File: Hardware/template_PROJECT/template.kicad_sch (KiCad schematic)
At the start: 7 parts

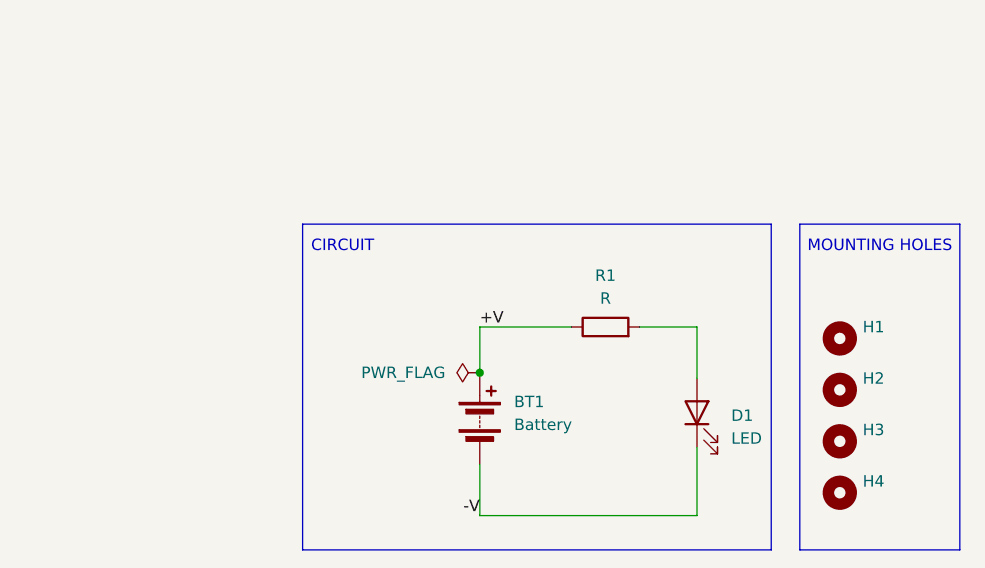
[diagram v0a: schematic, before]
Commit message: excluded mounting holes from bom and has an erc error i want to see what happens
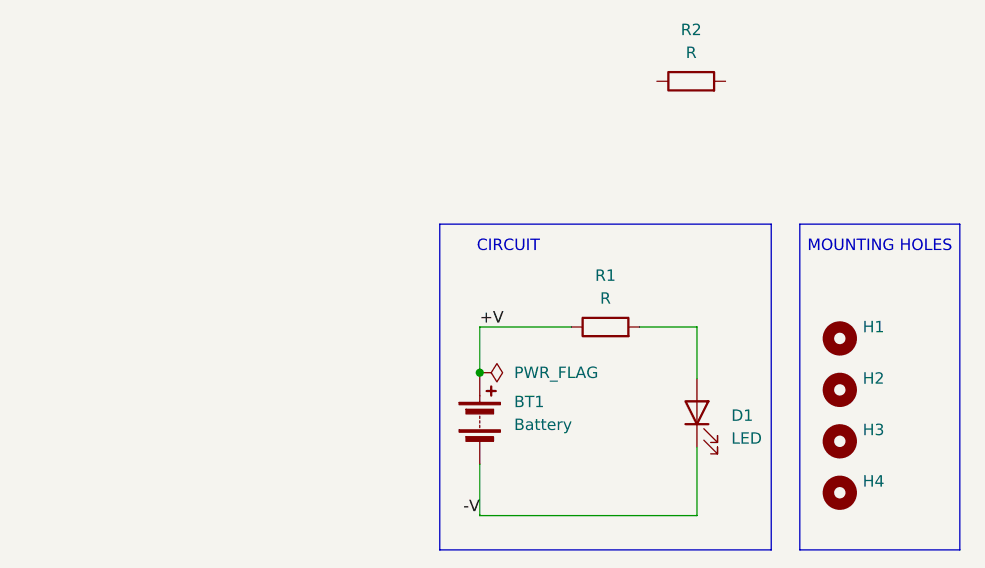
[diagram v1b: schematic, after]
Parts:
- added R2: R, Resistor_SMD:R_0805_2012Metric, symbol Device:R
- H1, H2, H3, H4: now left out of the parts list
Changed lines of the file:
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@@
 	)
 	(rectangle
-		(start 112.395 80.645)
+		(start 127.635 80.645)
 		(end 164.465 116.84)
 		(stroke
@@
 	(text "CIRCUIT"
 		(exclude_from_sim no)
-		(at 116.84 83.185 0)
+		(at 135.255 83.185 0)
 		(effects
 			(font
@@
 		(unit 1)
 		(exclude_from_sim no)
-		(in_bom yes)
+		(in_bom no)
 		(on_board yes)
 		(dnp no)
@@
 		(unit 1)
 		(exclude_from_sim no)
-		(in_bom yes)
+		(in_bom no)
 		(on_board yes)
 		(dnp no)
@@
 	(symbol
 		(lib_id "power:PWR_FLAG")
-		(at 132.08 97.155 90)
+		(at 132.08 97.155 270)
 		(unit 1)
 		(exclude_from_sim no)
@@
 		(fields_autoplaced yes)
 		(property "Reference" "#FLG01"
-			(at 130.175 97.155 0)
+			(at 133.985 97.155 0)
 			(effects
 				(font
@@
 		)
 		(property "Value" "PWR_FLAG"
-			(at 128.27 97.1549 90)
+			(at 135.89 97.1549 90)
 			(effects
 				(font
@@
 		(unit 1)
 		(exclude_from_sim no)
-		(in_bom yes)
+		(in_bom no)
 		(on_board yes)
 		(dnp no)
@@
 	)
 	(symbol
+		(lib_id "Device:R")
+		(at 155.575 64.77 90)
+		(unit 1)
+		(exclude_from_sim no)
+		(in_bom yes)
+		(on_board yes)
+		(dnp no)
+		(fields_autoplaced yes)
+		(property "Reference" "R2"
+			(at 155.575 59.055 90)
+			(effects
+				(font
+					(size 1.27 1.27)
+				)
+			)
+		)
+		(property "Value" "R"
+			(at 155.575 61.595 90)
+			(effects
+				(font
+					(size 1.27 1.27)
+				)
+			)
+		)
+		(property "Footprint" "Resistor_SMD:R_0805_2012Metric"
+			(at 155.575 66.548 90)
+			(effects
+				(font
+					(size 1.27 1.27)
+				)
+				(hide yes)
+			)
+		)
+		(property "Datasheet" "~"
+			(at 155.575 64.77 0)
+			(effects
+				(font
+					(size 1.27 1.27)
+				)
+				(hide yes)
+			)
+		)
+		(property "Description" "Resistor"
+			(at 155.575 64.77 0)
+			(effects
+				(font
+					(size 1.27 1.27)
+				)
+				(hide yes)
+			)
+		)
+		(pin "1"
+		)
+		(pin "2"
+		)
+		(instances
+			(project "template"
+				(path "/92a86815-0425-4ac3-80bb-037195814139"
+					(reference "R2")
+					(unit 1)
+				)
+			)
+		)
+	)
+	(symbol
 		(lib_id "Mechanical:MountingHole")
 		(at 172.085 99.06 0)
 		(unit 1)
 		(exclude_from_sim no)
-		(in_bom yes)
-		(on_board yes)
-		(dnp no)
+		(in_bom no)
+		(on_board yes)
+		(dnp no)

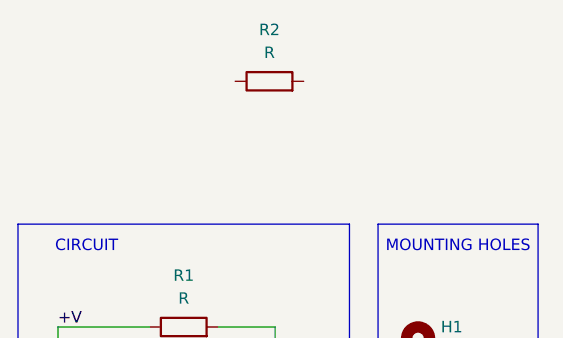
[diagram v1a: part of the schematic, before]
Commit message: should not longer error
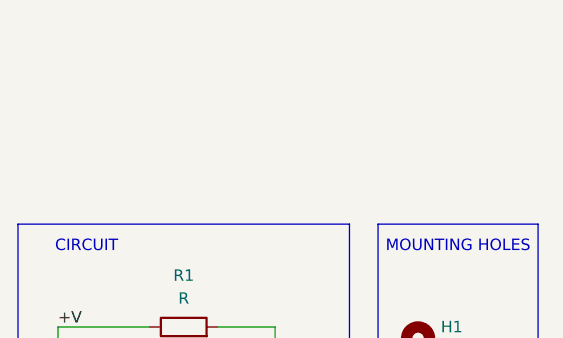
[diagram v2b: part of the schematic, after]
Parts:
- removed R2: R, Resistor_SMD:R_0805_2012Metric, symbol Device:R
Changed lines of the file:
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@@
-	)
-	(symbol
-		(lib_id "Device:R")
-		(at 155.575 64.77 90)
-		(unit 1)
-		(exclude_from_sim no)
-		(in_bom yes)
-		(on_board yes)
-		(dnp no)
-		(fields_autoplaced yes)
-		(property "Reference" "R2"
-			(at 155.575 59.055 90)
-			(effects
-				(font
-					(size 1.27 1.27)
-				)
-			)
-		)
-		(property "Value" "R"
-			(at 155.575 61.595 90)
-			(effects
-				(font
-					(size 1.27 1.27)
-				)
-			)
-		)
-		(property "Footprint" "Resistor_SMD:R_0805_2012Metric"
-			(at 155.575 66.548 90)
-			(effects
-				(font
-					(size 1.27 1.27)
-				)
-				(hide yes)
-			)
-		)
-		(property "Datasheet" "~"
-			(at 155.575 64.77 0)
-			(effects
-				(font
-					(size 1.27 1.27)
-				)
-				(hide yes)
-			)
-		)
-		(property "Description" "Resistor"
-			(at 155.575 64.77 0)
-			(effects
-				(font
-					(size 1.27 1.27)
-				)
-				(hide yes)
-			)
-		)
-		(pin "1"
-		)
-		(pin "2"
-		)
-		(instances
-			(project "template"
-				(path "/92a86815-0425-4ac3-80bb-037195814139"
-					(reference "R2")
-					(unit 1)
-				)
-			)
-		)
 	)
 	(symbol

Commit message: make it fail
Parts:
- added R2: R, Resistor_SMD:R_0805_2012Metric, symbol Device:R
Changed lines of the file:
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@@
+	)
+	(symbol
+		(lib_id "Device:R")
+		(at 105.41 95.885 90)
+		(unit 1)
+		(exclude_from_sim no)
+		(in_bom yes)
+		(on_board yes)
+		(dnp no)
+		(fields_autoplaced yes)
+		(property "Reference" "R2"
+			(at 105.41 90.17 90)
+			(effects
+				(font
+					(size 1.27 1.27)
+				)
+			)
+		)
+		(property "Value" "R"
+			(at 105.41 92.71 90)
+			(effects
+				(font
+					(size 1.27 1.27)
+				)
+			)
+		)
+		(property "Footprint" "Resistor_SMD:R_0805_2012Metric"
+			(at 105.41 97.663 90)
+			(effects
+				(font
+					(size 1.27 1.27)
+				)
+				(hide yes)
+			)
+		)
+		(property "Datasheet" "~"
+			(at 105.41 95.885 0)
+			(effects
+				(font
+					(size 1.27 1.27)
+				)
+				(hide yes)
+			)
+		)
+		(property "Description" "Resistor"
+			(at 105.41 95.885 0)
+			(effects
+				(font
+					(size 1.27 1.27)
+				)
+				(hide yes)
+			)
+		)
+		(pin "1"
+		)
+		(pin "2"
+		)
+		(instances
+			(project "template"
+				(path "/92a86815-0425-4ac3-80bb-037195814139"
+					(reference "R2")
+					(unit 1)
+				)
+			)
+		)
 	)
 	(symbol

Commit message: shouldnt fail now
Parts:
- removed R2: R, Resistor_SMD:R_0805_2012Metric, symbol Device:R
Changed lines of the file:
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@@
-	)
-	(symbol
-		(lib_id "Device:R")
-		(at 105.41 95.885 90)
-		(unit 1)
-		(exclude_from_sim no)
-		(in_bom yes)
-		(on_board yes)
-		(dnp no)
-		(fields_autoplaced yes)
-		(property "Reference" "R2"
-			(at 105.41 90.17 90)
-			(effects
-				(font
-					(size 1.27 1.27)
-				)
-			)
-		)
-		(property "Value" "R"
-			(at 105.41 92.71 90)
-			(effects
-				(font
-					(size 1.27 1.27)
-				)
-			)
-		)
-		(property "Footprint" "Resistor_SMD:R_0805_2012Metric"
-			(at 105.41 97.663 90)
-			(effects
-				(font
-					(size 1.27 1.27)
-				)
-				(hide yes)
-			)
-		)
-		(property "Datasheet" "~"
-			(at 105.41 95.885 0)
-			(effects
-				(font
-					(size 1.27 1.27)
-				)
-				(hide yes)
-			)
-		)
-		(property "Description" "Resistor"
-			(at 105.41 95.885 0)
-			(effects
-				(font
-					(size 1.27 1.27)
-				)
-				(hide yes)
-			)
-		)
-		(pin "1"
-		)
-		(pin "2"
-		)
-		(instances
-			(project "template"
-				(path "/92a86815-0425-4ac3-80bb-037195814139"
-					(reference "R2")
-					(unit 1)
-				)
-			)
-		)
 	)
 	(symbol

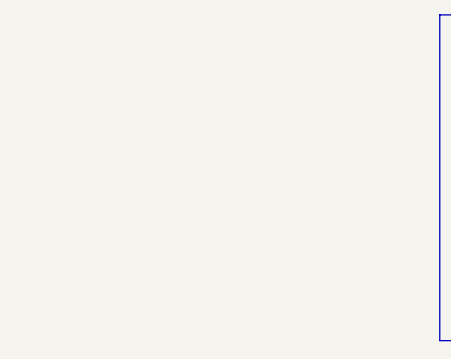
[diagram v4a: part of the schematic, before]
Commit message: needed it to fail erc
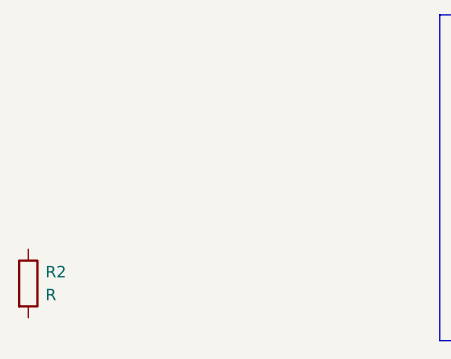
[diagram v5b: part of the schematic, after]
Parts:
- added R2: R, symbol Device:R
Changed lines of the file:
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@@
+		)
+	)
+	(symbol
+		(lib_id "Device:R")
+		(at 81.915 110.49 0)
+		(unit 1)
+		(exclude_from_sim no)
+		(in_bom yes)
+		(on_board yes)
+		(dnp no)
+		(fields_autoplaced yes)
+		(property "Reference" "R2"
+			(at 83.82 109.2199 0)
+			(effects
+				(font
+					(size 1.27 1.27)
+				)
+				(justify left)
+			)
+		)
+		(property "Value" "R"
+			(at 83.82 111.7599 0)
+			(effects
+				(font
+					(size 1.27 1.27)
+				)
+				(justify left)
+			)
+		)
+		(property "Footprint" ""
+			(at 80.137 110.49 90)
+			(effects
+				(font
+					(size 1.27 1.27)
+				)
+				(hide yes)
+			)
+		)
+		(property "Datasheet" "~"
+			(at 81.915 110.49 0)
+			(effects
+				(font
+					(size 1.27 1.27)
+				)
+				(hide yes)
+			)
+		)
+		(property "Description" "Resistor"
+			(at 81.915 110.49 0)
+			(effects
+				(font
+					(size 1.27 1.27)
+				)
+				(hide yes)
+			)
+		)
+		(pin "2"
+		)
+		(pin "1"
+		)
+		(instances
+			(project "template"
+				(path "/92a86815-0425-4ac3-80bb-037195814139"
+					(reference "R2")
+					(unit 1)
+				)
+			)
 		)
 	)

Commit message: i need more things to fail
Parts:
- R2: footprint (none) -> Resistor_SMD:R_0805_2012Metric
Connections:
- net -V: now also R2.1
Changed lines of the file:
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@@
 	(paper "A4")
+	(junction
+		(at 156.21 113.03)
+		(diameter 0)
+		(color 0 0 0 0)
+	)
 	(junction
 		(at 132.08 97.155)
@@
 	(symbol
 		(lib_id "Device:R")
-		(at 81.915 110.49 0)
+		(at 160.02 113.03 90)
 		(unit 1)
 		(exclude_from_sim no)
@@
 		(fields_autoplaced yes)
 		(property "Reference" "R2"
-			(at 83.82 109.2199 0)
-			(effects
-				(font
-					(size 1.27 1.27)
-				)
-				(justify left)
+			(at 160.02 107.315 90)
+			(effects
+				(font
+					(size 1.27 1.27)
+				)
 			)
 		)
 		(property "Value" "R"
-			(at 83.82 111.7599 0)
-			(effects
-				(font
-					(size 1.27 1.27)
-				)
-				(justify left)
-			)
-		)
-		(property "Footprint" ""
-			(at 80.137 110.49 90)
-			(effects
-				(font
-					(size 1.27 1.27)
-				)
-				(hide yes)
-			)
-		)
-		(property "Datasheet" "~"
-			(at 81.915 110.49 0)
+			(at 160.02 109.855 90)
+			(effects
+				(font
+					(size 1.27 1.27)
+				)
+			)
+		)
+		(property "Footprint" "Resistor_SMD:R_0805_2012Metric"
+			(at 160.02 114.808 90)
+			(effects
+				(font
+					(size 1.27 1.27)
+				)
+				(hide yes)
+			)
+		)
+		(property "Datasheet" "~"
+			(at 160.02 113.03 0)
 			(effects
 				(font
@@
 		)
 		(property "Description" "Resistor"
-			(at 81.915 110.49 0)
-			(effects
-				(font
-					(size 1.27 1.27)
-				)
-				(hide yes)
-			)
+			(at 160.02 113.03 0)
+			(effects
+				(font
+					(size 1.27 1.27)
+				)
+				(hide yes)
+			)
+		)
+		(pin "1"
 		)
 		(pin "2"
 		)
-		(pin "1"
-		)
-		(instances
+		(instances

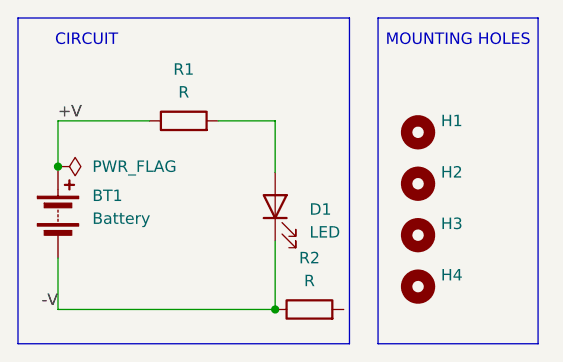
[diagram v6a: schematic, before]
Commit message: erc and drc should now pass
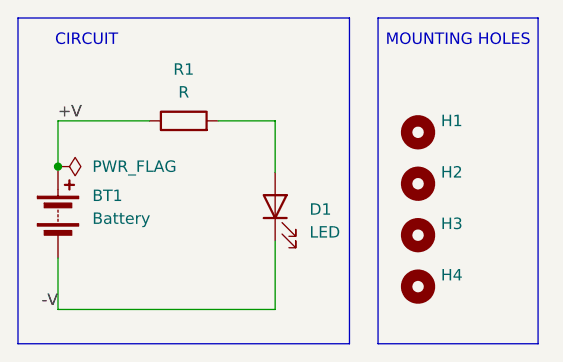
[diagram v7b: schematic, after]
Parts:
- removed R2: R, Resistor_SMD:R_0805_2012Metric, symbol Device:R
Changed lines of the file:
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@@
 	(paper "A4")
-	(junction
-		(at 156.21 113.03)
-		(diameter 0)
-		(color 0 0 0 0)
-	)
 	(junction
 		(at 132.08 97.155)
@@
 					(unit 1)
 				)
-			)
-		)
-	)
-	(symbol
-		(lib_id "Device:R")
-		(at 160.02 113.03 90)
-		(unit 1)
-		(exclude_from_sim no)
-		(in_bom yes)
-		(on_board yes)
-		(dnp no)
-		(fields_autoplaced yes)
-		(property "Reference" "R2"
-			(at 160.02 107.315 90)
-			(effects
-				(font
-					(size 1.27 1.27)
-				)
-			)
-		)
-		(property "Value" "R"
-			(at 160.02 109.855 90)
-			(effects
-				(font
-					(size 1.27 1.27)
-				)
-			)
-		)
-		(property "Footprint" "Resistor_SMD:R_0805_2012Metric"
-			(at 160.02 114.808 90)
-			(effects
-				(font
-					(size 1.27 1.27)
-				)
-				(hide yes)
-			)
-		)
-		(property "Datasheet" "~"
-			(at 160.02 113.03 0)
-			(effects
-				(font
-					(size 1.27 1.27)
-				)
-				(hide yes)
-			)
-		)
-		(property "Description" "Resistor"
-			(at 160.02 113.03 0)
-			(effects
-				(font
-					(size 1.27 1.27)
-				)
-				(hide yes)
-			)
-		)
-		(pin "1"
-		)
-		(pin "2"
-		)
-		(instances
-			(project "template"
-				(path "/92a86815-0425-4ac3-80bb-037195814139"
-					(reference "R2")
-					(unit 1)
-				)

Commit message: make em fail
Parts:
- added R2: R, Resistor_SMD:R_0805_2012Metric, symbol Device:R
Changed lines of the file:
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@@
+	)
+	(symbol
+		(lib_id "Device:R")
+		(at 115.57 92.075 90)
+		(unit 1)
+		(exclude_from_sim no)
+		(in_bom yes)
+		(on_board yes)
+		(dnp no)
+		(fields_autoplaced yes)
+		(property "Reference" "R2"
+			(at 115.57 86.36 90)
+			(effects
+				(font
+					(size 1.27 1.27)
+				)
+			)
+		)
+		(property "Value" "R"
+			(at 115.57 88.9 90)
+			(effects
+				(font
+					(size 1.27 1.27)
+				)
+			)
+		)
+		(property "Footprint" "Resistor_SMD:R_0805_2012Metric"
+			(at 115.57 93.853 90)
+			(effects
+				(font
+					(size 1.27 1.27)
+				)
+				(hide yes)
+			)
+		)
+		(property "Datasheet" "~"
+			(at 115.57 92.075 0)
+			(effects
+				(font
+					(size 1.27 1.27)
+				)
+				(hide yes)
+			)
+		)
+		(property "Description" "Resistor"
+			(at 115.57 92.075 0)
+			(effects
+				(font
+					(size 1.27 1.27)
+				)
+				(hide yes)
+			)
+		)
+		(pin "1"
+		)
+		(pin "2"
+		)
+		(instances
+			(project "template"
+				(path "/92a86815-0425-4ac3-80bb-037195814139"
+					(reference "R2")
+					(unit 1)
+				)
+			)
+		)
 	)
 	(symbol
